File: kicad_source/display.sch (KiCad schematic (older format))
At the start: 0 parts

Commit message: added flash, JTAG connector and display to schematic
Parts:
- added C? (x9): 1u 50V, capacitors:C_0603, symbol devices:C_0603
- added C?: 470n 50V, capacitors:C_0603, symbol devices:C_0603
- added CN?: CONN_01X24, symbol mechanical-connectors:CONN_01X24
- added D? (x3): MBR0530, symbol devices:D_Small
- added L?: INDUCTOR_SMALL, symbol devices:INDUCTOR_SMALL
- added Q?: SI1304BDL, symbol devices:Q_NMOS_GSD
- added R?: 2R2, resistors:R_0603, symbol devices:R_0603
- added R?: 0R, resistors:R_0603, symbol devices:R_0603
- added R?: DNI, resistors:R_0603, symbol devices:R_0603
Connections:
- net labels added: +3V3, BSI, DIS_BUSY, DIS_D_C#, DIS_RESET#, GDR, GND, RESE, SPI_CLK, SPI_CS_DIS, SPI_MOSI, TSCL, TSDA, VCOM, VDD, VGH, VGL, VPP, VSH1, VSH2, VSL
- wire segments 0 -> 66
- no-connect marks 0 -> 4
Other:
- note added: "select bus interface\nlow = 4 lines SPI (8 bit)\nhigh = 3 lines SPI (9 bit)"
- note added: "temperature sensor not used"

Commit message: added nfc part, generated schematic pdf
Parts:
- gave numbers to parts that had none: 19
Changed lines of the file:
@@
 $Descr A4 11693 8268
 encoding utf-8
-Sheet 3 6
-Title "snowfox-hw-business-card"
-Date "2020-05-07"
+Sheet 3 7
+Title "e-paper display"
+Date "2020-05-10"
 Rev "dev_0.1"
 Comp "generationmake"
@@
 $EndDescr
 $Comp
-L mechanical-connectors:CONN_01X24 CN?
+L mechanical-connectors:CONN_01X24 CN3
 U 1 1 5EC3DC2E
 P 8800 3550
-F 0 "CN?" H 8878 3591 50  0000 L CNN
+F 0 "CN3" H 8878 3591 50  0000 L CNN
 F 1 "CONN_01X24" H 8878 3500 50  0000 L CNN
 F 2 "" H 8800 3550 50  0000 C CNN
@@
 VCOM
 $Comp
-L power-supply:GND #PWR?
+L power-supply:GND #PWR053
 U 1 1 5EC457A9
 P 8550 4800
-F 0 "#PWR?" H 8550 4550 50  0001 C CNN
+F 0 "#PWR053" H 8550 4550 50  0001 C CNN
 F 1 "GND" H 8555 4627 50  0000 C CNN
 F 2 "" H 8550 4800 50  0000 C CNN
@@
 	8550 4000 8550 4800
 $Comp
-L devices:C_0603 C?
+L devices:C_0603 C25
 U 1 1 5EC469A1
 P 7050 2900
-F 0 "C?" H 7142 2946 50  0000 L CNN
+F 0 "C25" H 7142 2946 50  0000 L CNN
 F 1 "1u 50V" H 7142 2855 50  0000 L CNN
 F 2 "capacitors:C_0603" H 7050 2750 50  0001 C CNN
@@
 $EndComp
 $Comp
-L power-supply:GND #PWR?
+L power-supply:GND #PWR049
 U 1 1 5EC46F89
 P 7050 3050
-F 0 "#PWR?" H 7050 2800 50  0001 C CNN
+F 0 "#PWR049" H 7050 2800 50  0001 C CNN
 F 1 "GND" H 7055 2877 50  0000 C CNN
 F 2 "" H 7050 3050 50  0000 C CNN
@@
 	7050 3000 7050 3050
 $Comp
-L devices:C_0603 C?
+L devices:C_0603 C27
 U 1 1 5EC47E9F
 P 7950 4800
-F 0 "C?" H 8042 4846 50  0000 L CNN
+F 0 "C27" H 8042 4846 50  0000 L CNN
 F 1 "470n 50V" H 8042 4755 50  0000 L CNN
 F 2 "capacitors:C_0603" H 7950 4650 50  0001 C CNN
@@
 $EndComp
 $Comp
-L devices:C_0603 C?
+L devices:C_0603 C26
 U 1 1 5EC4889C
 P 7450 4800
-F 0 "C?" H 7542 4846 50  0000 L CNN
+F 0 "C26" H 7542 4846 50  0000 L CNN
 F 1 "1u 50V" H 7542 4755 50  0000 L CNN
 F 2 "capacitors:C_0603" H 7450 4650 50  0001 C CNN
@@
 $EndComp
 $Comp
-L devices:C_0603 C?
+L devices:C_0603 C24
 U 1 1 5EC49C80
 P 6950 4800
-F 0 "C?" H 7042 4846 50  0000 L CNN
+F 0 "C24" H 7042 4846 50  0000 L CNN
 F 1 "1u 50V" H 7042 4755 50  0000 L CNN
 F 2 "capacitors:C_0603" H 6950 4650 50  0001 C CNN
@@
 $EndComp
 $Comp
-L devices:C_0603 C?
+L devices:C_0603 C23
 U 1 1 5EC49EFA
 P 6500 4800
-F 0 "C?" H 6592 4846 50  0000 L CNN
+F 0 "C23" H 6592 4846 50  0000 L CNN
 F 1 "1u 50V" H 6592 4755 50  0000 L CNN
 F 2 "capacitors:C_0603" H 6500 4650 50  0001 C CNN
@@
 $EndComp
 $Comp
-L devices:C_0603 C?
+L devices:C_0603 C22
 U 1 1 5EC4A536
 P 6000 4800
-F 0 "C?" H 6092 4846 50  0000 L CNN
+F 0 "C22" H 6092 4846 50  0000 L CNN
 F 1 "1u 50V" H 6092 4755 50  0000 L CNN
 F 2 "capacitors:C_0603" H 6000 4650 50  0001 C CNN
@@
 $EndComp
 $Comp
-L power-supply:GND #PWR?
+L power-supply:GND #PWR052
 U 1 1 5EC4B0A2
 P 7950 4950
-F 0 "#PWR?" H 7950 4700 50  0001 C CNN
+F 0 "#PWR052" H 7950 4700 50  0001 C CNN
 F 1 "GND" H 7955 4777 50  0000 C CNN
 F 2 "" H 7950 4950 50  0000 C CNN
@@
 $EndComp
 $Comp
-L power-supply:GND #PWR?
+L power-supply:GND #PWR050
 U 1 1 5EC4B2A6
 P 7450 4950
-F 0 "#PWR?" H 7450 4700 50  0001 C CNN
+F 0 "#PWR050" H 7450 4700 50  0001 C CNN
 F 1 "GND" H 7455 4777 50  0000 C CNN
 F 2 "" H 7450 4950 50  0000 C CNN
@@
 $EndComp
 $Comp
-L power-supply:GND #PWR?
+L power-supply:GND #PWR048
 U 1 1 5EC4B4D4
 P 6950 4950
-F 0 "#PWR?" H 6950 4700 50  0001 C CNN
+F 0 "#PWR048" H 6950 4700 50  0001 C CNN
 F 1 "GND" H 6955 4777 50  0000 C CNN
 F 2 "" H 6950 4950 50  0000 C CNN
@@
 $EndComp
 $Comp
-L power-supply:GND #PWR?
+L power-supply:GND #PWR045
 U 1 1 5EC4B720
 P 6500 4950
-F 0 "#PWR?" H 6500 4700 50  0001 C CNN
+F 0 "#PWR045" H 6500 4700 50  0001 C CNN
 F 1 "GND" H 6505 4777 50  0000 C CNN
 F 2 "" H 6500 4950 50  0000 C CNN
@@
 $EndComp
 $Comp
-L power-supply:GND #PWR?
+L power-supply:GND #PWR044
 U 1 1 5EC4B930
 P 6000 4950
-F 0 "#PWR?" H 6000 4700 50  0001 C CNN
+F 0 "#PWR044" H 6000 4700 50  0001 C CNN
 F 1 "GND" H 6005 4777 50  0000 C CNN
 F 2 "" H 6000 4950 50  0000 C CNN
@@
 	7950 4900 7950 4950
 $Comp
-L devices:R_0603 R?
+L devices:R_0603 R15
 U 1 1 5EC543D9
 P 4350 4150
-F 0 "R?" H 4409 4196 50  0000 L CNN
+F 0 "R15" H 4409 4196 50  0000 L CNN
 F 1 "2R2" H 4409 4105 50  0000 L CNN
 F 2 "resistors:R_0603" H 4350 4000 50  0001 C CNN
@@
 $EndComp
 $Comp
-L power-supply:GND #PWR?
+L power-supply:GND #PWR042
 U 1 1 5EC546D2
 P 4350 4300
-F 0 "#PWR?" H 4350 4050 50  0001 C CNN
+F 0 "#PWR042" H 4350 4050 50  0001 C CNN
 F 1 "GND" H 4355 4127 50  0000 C CNN
 F 2 "" H 4350 4300 50  0000 C CNN
@@
 $EndComp
 $Comp
-L devices:Q_NMOS_GSD Q?
+L devices:Q_NMOS_GSD Q1
 U 1 1 5EC54BFE
 P 4250 3750
-F 0 "Q?" H 4440 3796 50  0000 L CNN
+F 0 "Q1" H 4440 3796 50  0000 L CNN
 F 1 "SI1304BDL" H 4440 3705 50  0000 L CNN
 F 2 "" H 4450 3850 50  0000 C CNN
@@
 	4350 4250 4350 4300
 $Comp
-L devices:INDUCTOR_SMALL L?
+L devices:INDUCTOR_SMALL L1
 U 1 1 5EC574C4
 P 4000 3350
-F 0 "L?" H 4000 3565 50  0000 C CNN
+F 0 "L1" H 4000 3565 50  0000 C CNN
 F 1 "INDUCTOR_SMALL" H 4000 3474 50  0000 C CNN
 F 2 "" H 4000 3350 50  0000 C CNN
@@
 $EndComp
 $Comp
-L devices:D_Small D?
+L devices:D_Small D4
 U 1 1 5EC57B54
 P 4850 3350
-F 0 "D?" H 4850 3145 50  0000 C CNN
+F 0 "D4" H 4850 3145 50  0000 C CNN
 F 1 "MBR0530" H 4850 3236 50  0000 C CNN
 F 2 "" V 4850 3350 50  0000 C CNN
@@
 $EndComp
 $Comp
-L devices:C_0603 C?
+L devices:C_0603 C20
 U 1 1 5EC584A5
 P 4350 2850
-F 0 "C?" H 4442 2896 50  0000 L CNN
+F 0 "C20" H 4442 2896 50  0000 L CNN
 F 1 "1u 50V" H 4442 2805 50  0000 L CNN
 F 2 "capacitors:C_0603" H 4350 2700 50  0001 C CNN
@@
 $EndComp
 $Comp
-L devices:C_0603 C?
+L devices:C_0603 C21
 U 1 1 5EC58C85
 P 5200 2850
-F 0 "C?" H 5292 2896 50  0000 L CNN
+F 0 "C21" H 5292 2896 50  0000 L CNN
 F 1 "1u 50V" H 5292 2805 50  0000 L CNN
 F 2 "capacitors:C_0603" H 5200 2700 50  0001 C CNN
@@
 $EndComp
 $Comp
-L devices:C_0603 C?
+L devices:C_0603 C19
 U 1 1 5EC5BBE6
 P 3400 2850
-F 0 "C?" H 3492 2896 50  0000 L CNN
+F 0 "C19" H 3492 2896 50  0000 L CNN
 F 1 "1u 50V" H 3492 2805 50  0000 L CNN
 F 2 "capacitors:C_0603" H 3400 2700 50  0001 C CNN
@@
 $EndComp
 $Comp
-L power-supply:GND #PWR?
+L power-supply:GND #PWR041
 U 1 1 5EC5BEBA
 P 3400 3000
-F 0 "#PWR?" H 3400 2750 50  0001 C CNN
+F 0 "#PWR041" H 3400 2750 50  0001 C CNN
 F 1 "GND" H 3405 2827 50  0000 C CNN
 F 2 "" H 3400 3000 50  0000 C CNN
@@
 $EndComp
 $Comp
-L devices:C_0603 C?
+L devices:C_0603 C18
 U 1 1 5EC5C3F9
 P 2950 3500
-F 0 "C?" H 3042 3546 50  0000 L CNN
+F 0 "C18" H 3042 3546 50  0000 L CNN
 F 1 "1u 50V" H 3042 3455 50  0000 L CNN
 F 2 "capacitors:C_0603" H 2950 3350 50  0001 C CNN
@@
 $EndComp
 $Comp
-L power-supply:GND #PWR?
+L power-supply:GND #PWR040
 U 1 1 5EC5C670
 P 2950 3650
-F 0 "#PWR?" H 2950 3400 50  0001 C CNN
+F 0 "#PWR040" H 2950 3400 50  0001 C CNN
 F 1 "GND" H 2955 3477 50  0000 C CNN
 F 2 "" H 2950 3650 50  0000 C CNN
@@
 $EndComp
 $Comp
-L power-supply:GND #PWR?
+L power-supply:GND #PWR043
 U 1 1 5EC5CC35
 P 5350 2600
-F 0 "#PWR?" H 5350 2350 50  0001 C CNN
+F 0 "#PWR043" H 5350 2350 50  0001 C CNN
 F 1 "GND" V 5355 2472 50  0000 R CNN
 F 2 "" H 5350 2600 50  0000 C CNN
@@
 $EndComp
 $Comp
-L devices:D_Small D?
+L devices:D_Small D3
 U 1 1 5EC5D0DA
 P 4850 2600
-F 0 "D?" H 4850 2395 50  0000 C CNN
+F 0 "D3" H 4850 2395 50  0000 C CNN
 F 1 "MBR0530" H 4850 2486 50  0000 C CNN
 F 2 "" V 4850 2600 50  0000 C CNN
@@
 $EndComp
 $Comp
-L devices:D_Small D?
+L devices:D_Small D2
 U 1 1 5EC5D3FB
 P 3900 2600
-F 0 "D?" H 3900 2395 50  0000 C CNN
+F 0 "D2" H 3900 2395 50  0000 C CNN
 F 1 "MBR0530" H 3900 2486 50  0000 C CNN
 F 2 "" V 3900 2600 50  0000 C CNN
@@
 temperature sensor not used
 $Comp
-L devices:R_0603 R?
+L devices:R_0603 R17
 U 1 1 5EC7BF40
 P 6800 2100
-F 0 "R?" H 6859 2146 50  0000 L CNN
+F 0 "R17" H 6859 2146 50  0000 L CNN
 F 1 "0R" H 6859 2055 50  0000 L CNN
 F 2 "resistors:R_0603" H 6800 1950 50  0001 C CNN
@@
 $EndComp
 $Comp
-L devices:R_0603 R?
+L devices:R_0603 R16
 U 1 1 5EC7D039
 P 6800 1800
-F 0 "R?" H 6859 1846 50  0000 L CNN
+F 0 "R16" H 6859 1846 50  0000 L CNN
 F 1 "DNI" H 6859 1755 50  0000 L CNN
 F 2 "resistors:R_0603" H 6800 1650 50  0001 C CNN
@@
 $EndComp
 $Comp
-L power-supply:GND #PWR?
+L power-supply:GND #PWR047
 U 1 1 5EC7D34F
 P 6800 2250
-F 0 "#PWR?" H 6800 2000 50  0001 C CNN
+F 0 "#PWR047" H 6800 2000 50  0001 C CNN
 F 1 "GND" H 6805 2077 50  0000 C CNN
 F 2 "" H 6800 2250 50  0000 C CNN
@@
 $EndComp
 $Comp
-L power-supply:+3V3 #PWR?
+L power-supply:+3V3 #PWR046
 U 1 1 5EC7D845
 P 6800 1650
-F 0 "#PWR?" H 6800 1500 50  0001 C CNN
+F 0 "#PWR046" H 6800 1500 50  0001 C CNN
 F 1 "+3V3" H 6815 1823 50  0000 C CNN
 F 2 "" H 6800 1650 50  0000 C CNN
@@
 select bus interface\nlow = 4 lines SPI (8 bit)\nhigh = 3 lines SPI (9 bit)
 $Comp
-L power-supply:+3V3 #PWR?
+L power-supply:+3V3 #PWR051
 U 1 1 5EC86890
 P 7750 3900
-F 0 "#PWR?" H 7750 3750 50  0001 C CNN
+F 0 "#PWR051" H 7750 3750 50  0001 C CNN
 F 1 "+3V3" V 7765 4028 50  0000 L CNN
 F 2 "" H 7750 3900 50  0000 C CNN
@@
 $EndComp
 $Comp
-L power-supply:+3V3 #PWR?
+L power-supply:+3V3 #PWR039
 U 1 1 5EC87185
 P 2400 3350
-F 0 "#PWR?" H 2400 3200 50  0001 C CNN
+F 0 "#PWR039" H 2400 3200 50  0001 C CNN
 F 1 "+3V3" V 2415 3478 50  0000 L CNN
 F 2 "" H 2400 3350 50  0000 C CNN

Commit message: started placement
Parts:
- CN3: footprint (none) -> pin_headers:Pin_Header_Angled_1x24_Pitch1.00mm
- D2, D3, D4: footprint (none) -> diodes:SOD-123
- L1: footprint (none) -> inductors:Inductor_1212
- Q1: footprint (none) -> SOT_TO:SOT-23
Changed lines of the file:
@@
 F 0 "CN3" H 8878 3591 50  0000 L CNN
 F 1 "CONN_01X24" H 8878 3500 50  0000 L CNN
-F 2 "" H 8800 3550 50  0000 C CNN
+F 2 "pin_headers:Pin_Header_Angled_1x24_Pitch1.00mm" H 8800 3550 50  0001 C CNN
 F 3 "" H 8800 3550 50  0000 C CNN
 	1    8800 3550
@@
 F 0 "Q1" H 4440 3796 50  0000 L CNN
 F 1 "SI1304BDL" H 4440 3705 50  0000 L CNN
-F 2 "" H 4450 3850 50  0000 C CNN
+F 2 "SOT_TO:SOT-23" H 4450 3850 50  0001 C CNN
 F 3 "" H 4250 3750 50  0000 C CNN
 	1    4250 3750
@@
 F 0 "L1" H 4000 3565 50  0000 C CNN
 F 1 "INDUCTOR_SMALL" H 4000 3474 50  0000 C CNN
-F 2 "" H 4000 3350 50  0000 C CNN
+F 2 "inductors:Inductor_1212" H 4000 3350 50  0001 C CNN
 F 3 "" H 4000 3350 50  0000 C CNN
 	1    4000 3350
@@
 F 0 "D4" H 4850 3145 50  0000 C CNN
 F 1 "MBR0530" H 4850 3236 50  0000 C CNN
-F 2 "" V 4850 3350 50  0000 C CNN
+F 2 "diodes:SOD-123" V 4850 3350 50  0001 C CNN
 F 3 "" V 4850 3350 50  0000 C CNN
 	1    4850 3350
@@
 F 0 "D3" H 4850 2395 50  0000 C CNN
 F 1 "MBR0530" H 4850 2486 50  0000 C CNN
-F 2 "" V 4850 2600 50  0000 C CNN
+F 2 "diodes:SOD-123" V 4850 2600 50  0001 C CNN
 F 3 "" V 4850 2600 50  0000 C CNN
 	1    4850 2600
@@
 F 0 "D2" H 3900 2395 50  0000 C CNN
 F 1 "MBR0530" H 3900 2486 50  0000 C CNN
-F 2 "" V 3900 2600 50  0000 C CNN
+F 2 "diodes:SOD-123" V 3900 2600 50  0001 C CNN
 F 3 "" V 3900 2600 50  0000 C CNN
 	1    3900 2600

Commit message: changed connector for display
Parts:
- CN3: footprint pin_headers:Pin_Header_Angled_1x24_Pitch1.00mm -> CON_wuerth:WR-FPC_68712414522
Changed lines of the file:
@@
 F 0 "CN3" H 8878 3591 50  0000 L CNN
 F 1 "CONN_01X24" H 8878 3500 50  0000 L CNN
-F 2 "pin_headers:Pin_Header_Angled_1x24_Pitch1.00mm" H 8800 3550 50  0001 C CNN
+F 2 "CON_wuerth:WR-FPC_68712414522" H 8800 3550 50  0001 C CNN
 F 3 "" H 8800 3550 50  0000 C CNN
 	1    8800 3550

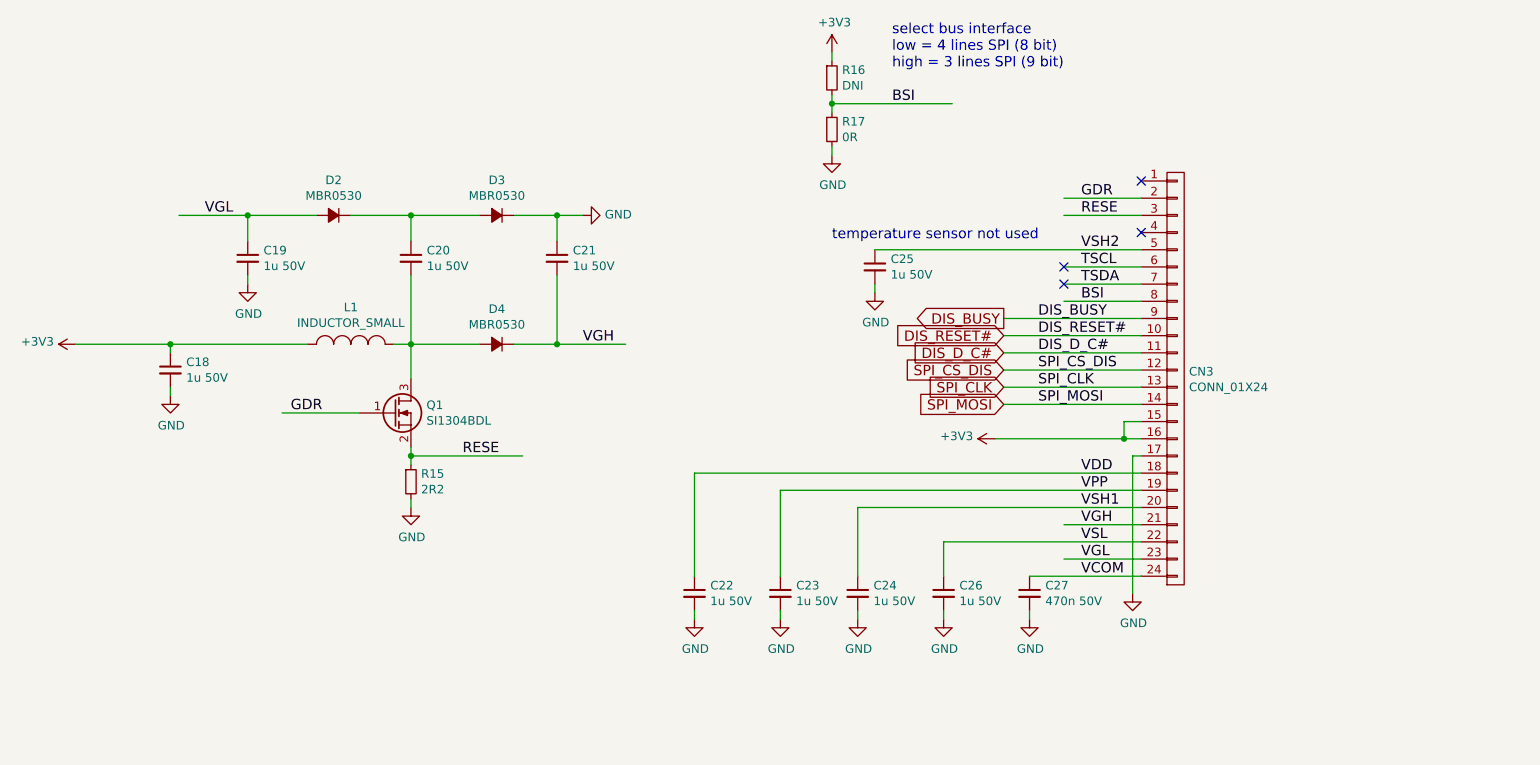
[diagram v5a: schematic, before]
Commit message: updated schematic pdf and renderings
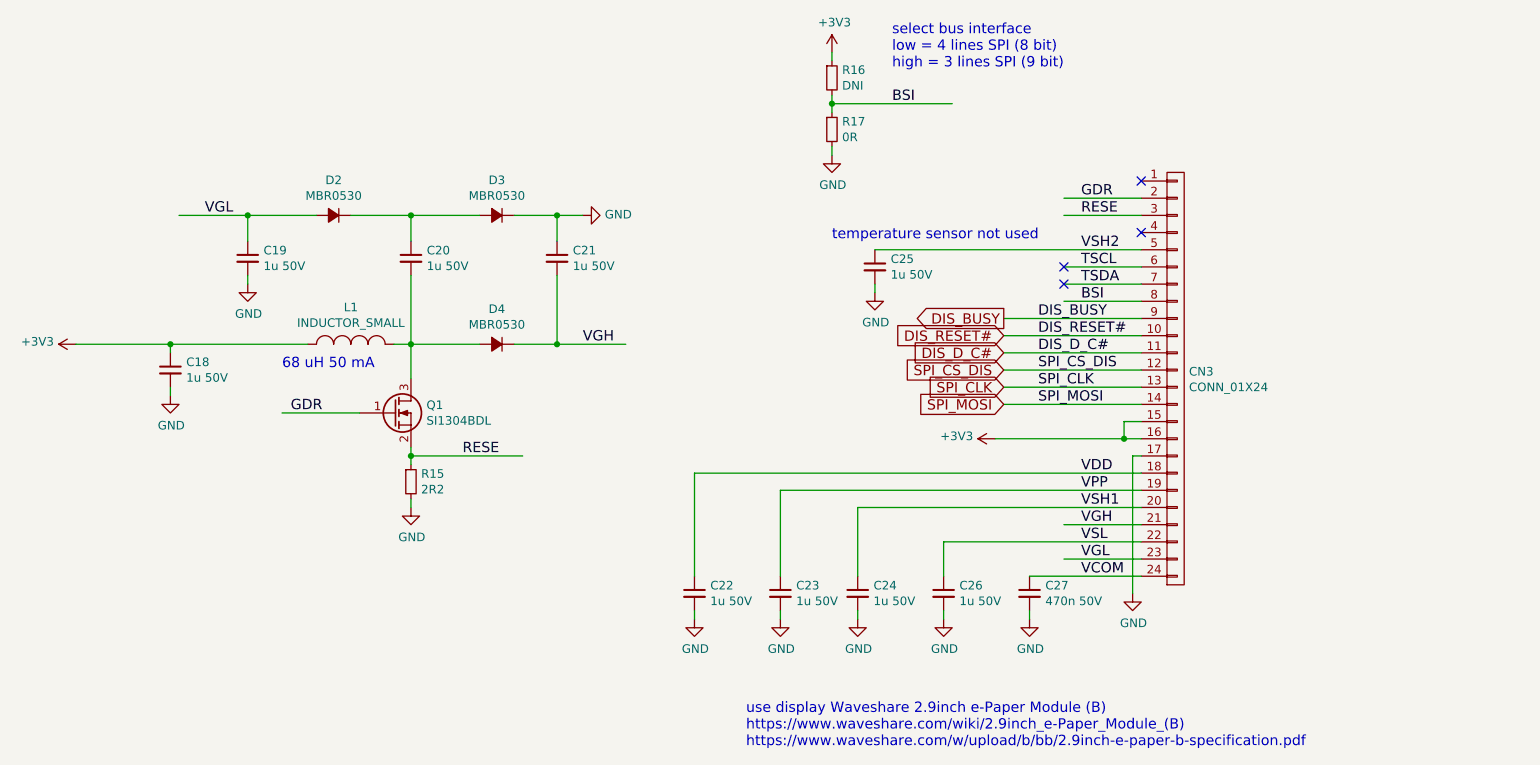
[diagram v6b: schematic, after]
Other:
- note added: "68 uH 50 mA"
- note added: "use display Waveshare 2.9inch e-Paper Module (B)\nhttps://www.waveshare.com/wiki/2.9inch_e-Paper_Module_(B)\nhttps://www.waveshare.com/w/upload/b/bb/2.9inch-e-paper-b-specification.pdf"
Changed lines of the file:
@@
 Text GLabel 7800 3400 0    60   Input ~ 0
 DIS_D_C#
+Text Notes 6300 5700 0    60   ~ 0
+use display Waveshare 2.9inch e-Paper Module (B)\nhttps://www.waveshare.com/wiki/2.9inch_e-Paper_Module_(B)\nhttps://www.waveshare.com/w/upload/b/bb/2.9inch-e-paper-b-specification.pdf
+Text Notes 3600 3500 0    60   ~ 0
+68 uH 50 mA
 $EndSCHEMATC

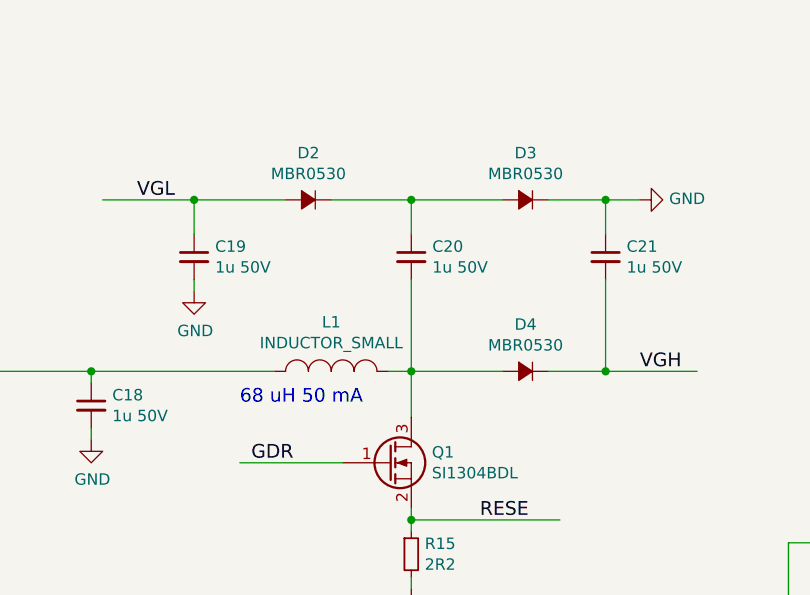
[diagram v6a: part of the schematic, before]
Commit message: changed diodes to smaller footprint, connected all lines in layout, updated images
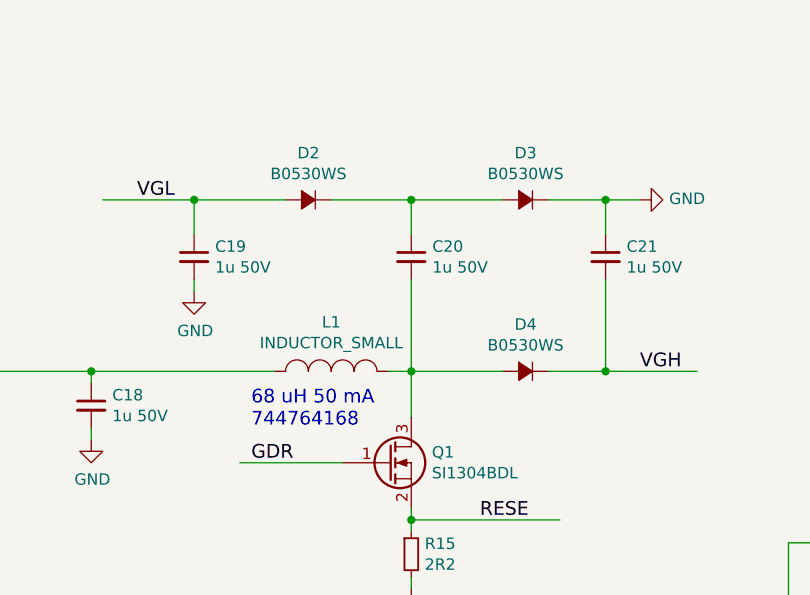
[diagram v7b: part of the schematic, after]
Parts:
- D2, D3, D4: value MBR0530 -> B0530WS; footprint diodes:SOD-123 -> diodes:SOD-323
- L1: footprint inductors:Inductor_1212 -> resistors:R_1210
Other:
- note added: "68 uH 50 mA\n744764168"
- note removed: "68 uH 50 mA"
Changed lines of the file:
@@
 F 0 "L1" H 4000 3565 50  0000 C CNN
 F 1 "INDUCTOR_SMALL" H 4000 3474 50  0000 C CNN
-F 2 "inductors:Inductor_1212" H 4000 3350 50  0001 C CNN
+F 2 "resistors:R_1210" H 4000 3350 50  0001 C CNN
 F 3 "" H 4000 3350 50  0000 C CNN
 	1    4000 3350
@@
 P 4850 3350
 F 0 "D4" H 4850 3145 50  0000 C CNN
-F 1 "MBR0530" H 4850 3236 50  0000 C CNN
-F 2 "diodes:SOD-123" V 4850 3350 50  0001 C CNN
+F 1 "B0530WS" H 4850 3236 50  0000 C CNN
+F 2 "diodes:SOD-323" V 4850 3350 50  0001 C CNN
 F 3 "" V 4850 3350 50  0000 C CNN
 	1    4850 3350
@@
 P 4850 2600
 F 0 "D3" H 4850 2395 50  0000 C CNN
-F 1 "MBR0530" H 4850 2486 50  0000 C CNN
-F 2 "diodes:SOD-123" V 4850 2600 50  0001 C CNN
+F 1 "B0530WS" H 4850 2486 50  0000 C CNN
+F 2 "diodes:SOD-323" V 4850 2600 50  0001 C CNN
 F 3 "" V 4850 2600 50  0000 C CNN
 	1    4850 2600
@@
 P 3900 2600
 F 0 "D2" H 3900 2395 50  0000 C CNN
-F 1 "MBR0530" H 3900 2486 50  0000 C CNN
-F 2 "diodes:SOD-123" V 3900 2600 50  0001 C CNN
+F 1 "B0530WS" H 3900 2486 50  0000 C CNN
+F 2 "diodes:SOD-323" V 3900 2600 50  0001 C CNN
 F 3 "" V 3900 2600 50  0000 C CNN
 	1    3900 2600
@@
 Text Notes 6300 5700 0    60   ~ 0
 use display Waveshare 2.9inch e-Paper Module (B)\nhttps://www.waveshare.com/wiki/2.9inch_e-Paper_Module_(B)\nhttps://www.waveshare.com/w/upload/b/bb/2.9inch-e-paper-b-specification.pdf
-Text Notes 3600 3500 0    60   ~ 0
-68 uH 50 mA
+Text Notes 3650 3600 0    60   ~ 0
+68 uH 50 mA\n744764168
 $EndSCHEMATC
